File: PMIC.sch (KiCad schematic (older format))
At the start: 20 parts, among them J6 USB_B_Micro, U4 STPMIC1APQR

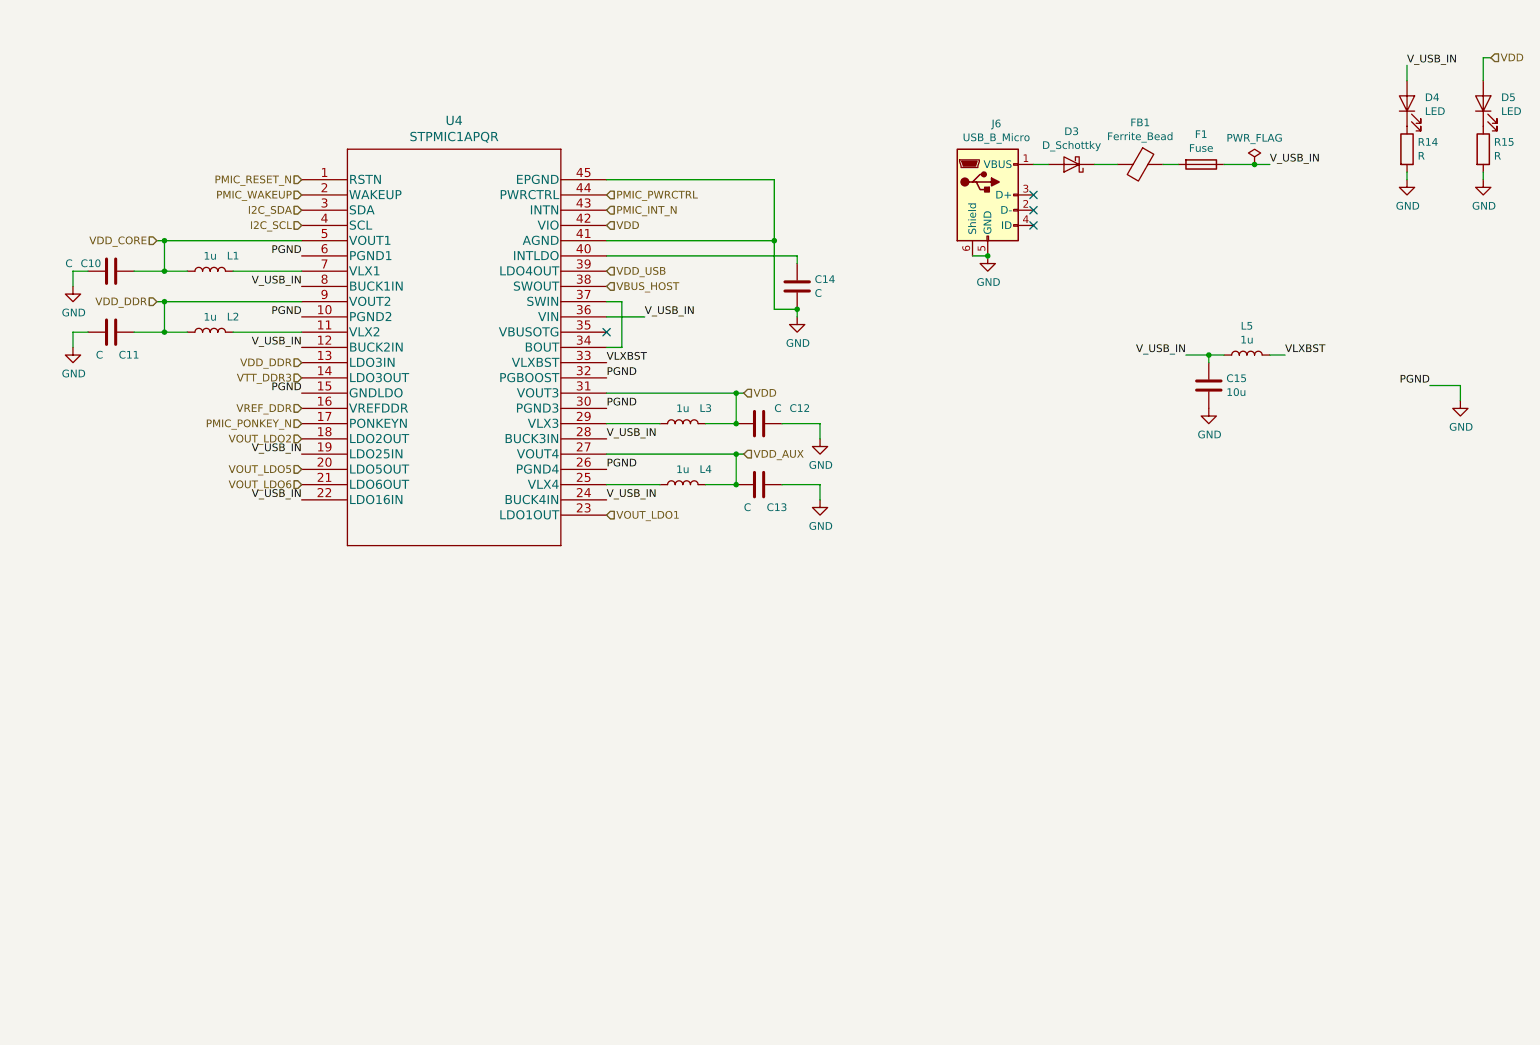
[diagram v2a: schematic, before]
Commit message: Complete ethernet and PMIC circuitry
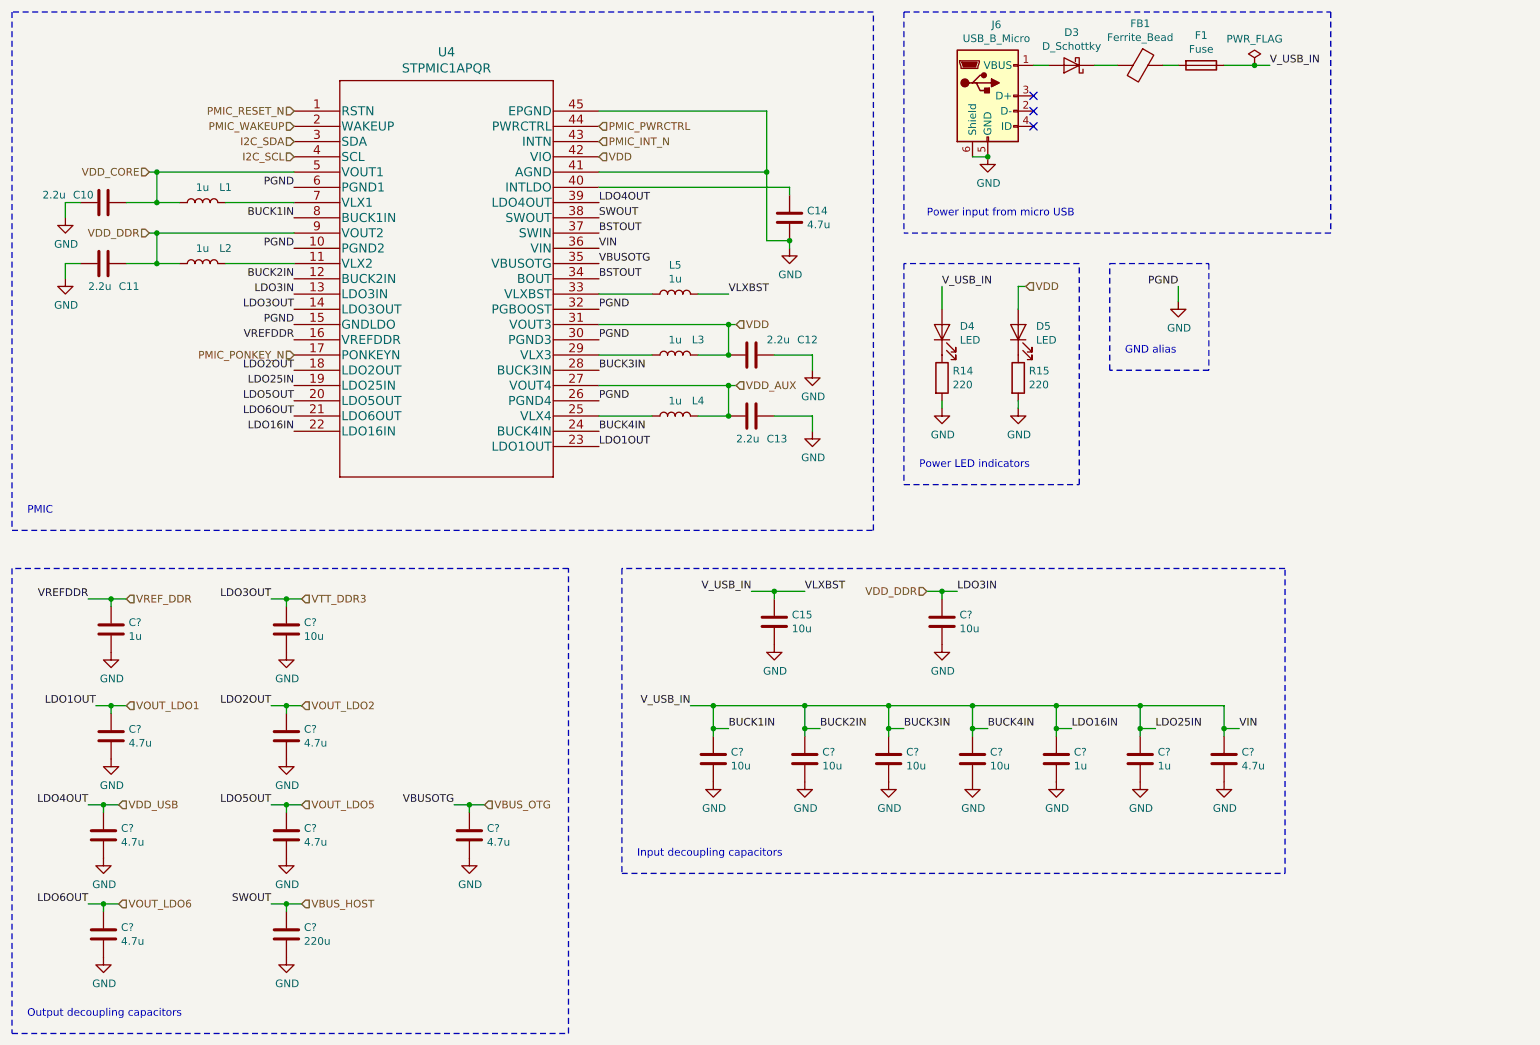
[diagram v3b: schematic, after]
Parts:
- added C? (x4): 10u, Capacitor_SMD:C_0603_1608Metric, symbol Device:C
- added C? (x7): 4.7u, symbol Device:C
- added C?: 220u, symbol Device:C
- added C? (x3): 1u, symbol Device:C
- added C? (x2): 10u, symbol Device:C
- C10, C11, C12, C13: value C -> 2.2u
- C14: value C -> 4.7u
- R14, R15: value R -> 220
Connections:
- net GND: now also C?.2, C?.2, C?.2, C?.2, C?.2, C?.2, C?.2, C?.2, C?.2, C?.2, C?.2, C?.2, C?.2, C?.2, C?.2, C?.2, C?.2
- net VBUS_HOST: now also C?.1
- net VDD_DDR: now also C?.1
- net VDD_USB: now also C?.1
- net VOUT_LDO1: now also C?.1
- net VOUT_LDO2: now also C?.1
- net VOUT_LDO5: now also C?.1
- net VOUT_LDO6: now also C?.1
- net VREF_DDR: now also C?.1
- net VTT_DDR3: now also C?.1
- net BSTOUT: now reaches U4.34 (BOUT), U4.37 (SWIN)
- net VBUS_OTG: now reaches U4.35 (VBUSOTG)
- net VBUS_OTG: now also C?.1
- net VLXBST: no longer names the net of U4.33 (VLXBST)
- net VLXBST: now also L5.1; no longer L5.2
- net V_USB_IN renamed BUCK1IN
- net BUCK1IN: now also L5.2, C?.1, C?.1, C?.1, C?.1, C?.1, C?.1, C?.1; no longer L5.1
- no-connect marks 4 -> 3
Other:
- note added: "GND alias\n"
- note added: "Input decoupling capacitors\n"
- note added: "Output decoupling capacitors"
- note added: "PMIC\n"
- note added: "Power LED indicators"
- note added: "Power input from micro USB"
- moved on the sheet: C10, C11, C12, C13, C14, C15, D3, D4, D5, F1, FB1, J6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

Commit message: Finish labelling RAM
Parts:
- gave numbers to parts that had none: 17
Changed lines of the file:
@@
 SWOUT
 $Comp
-L Device:C C?
+L Device:C C77
 U 1 1 616DE826
 P 5700 5650
-F 0 "C?" H 5815 5696 50  0000 L CNN
+F 0 "C77" H 5815 5696 50  0000 L CNN
 F 1 "10u" H 5815 5605 50  0000 L CNN
 F 2 "Capacitor_SMD:C_0603_1608Metric" H 5738 5500 50  0001 C CNN
@@
 V_USB_IN
 $Comp
-L power:GND #PWR?
+L power:GND #PWR0111
 U 1 1 616DE831
 P 5700 5800
-F 0 "#PWR?" H 5700 5550 50  0001 C CNN
+F 0 "#PWR0111" H 5700 5550 50  0001 C CNN
 F 1 "GND" H 5705 5627 50  0000 C CNN
 F 2 "" H 5700 5800 50  0001 C CNN
@@
 BUCK1IN
 $Comp
-L Device:C C?
+L Device:C C78
 U 1 1 616E9957
 P 6300 5650
-F 0 "C?" H 6415 5696 50  0000 L CNN
+F 0 "C78" H 6415 5696 50  0000 L CNN
 F 1 "10u" H 6415 5605 50  0000 L CNN
 F 2 "Capacitor_SMD:C_0603_1608Metric" H 6338 5500 50  0001 C CNN
@@
 	6300 5450 6400 5450
 $Comp
-L power:GND #PWR?
+L power:GND #PWR0112
 U 1 1 616E9962
 P 6300 5800
-F 0 "#PWR?" H 6300 5550 50  0001 C CNN
+F 0 "#PWR0112" H 6300 5550 50  0001 C CNN
 F 1 "GND" H 6305 5627 50  0000 C CNN
 F 2 "" H 6300 5800 50  0001 C CNN
@@
 Connection ~ 6300 5450
 $Comp
-L Device:C C?
+L Device:C C79
 U 1 1 616F4A5E
 P 6850 5650
-F 0 "C?" H 6965 5696 50  0000 L CNN
+F 0 "C79" H 6965 5696 50  0000 L CNN
 F 1 "10u" H 6965 5605 50  0000 L CNN
 F 2 "Capacitor_SMD:C_0603_1608Metric" H 6888 5500 50  0001 C CNN
@@
 	6850 5450 6950 5450
 $Comp
-L power:GND #PWR?
+L power:GND #PWR0113
 U 1 1 616F4A66
 P 6850 5800
-F 0 "#PWR?" H 6850 5550 50  0001 C CNN
+F 0 "#PWR0113" H 6850 5550 50  0001 C CNN
 F 1 "GND" H 6855 5627 50  0000 C CNN
 F 2 "" H 6850 5800 50  0001 C CNN
@@
 Connection ~ 6850 5450
 $Comp
-L Device:C C?
+L Device:C C81
 U 1 1 616F6459
 P 7400 5650
-F 0 "C?" H 7515 5696 50  0000 L CNN
+F 0 "C81" H 7515 5696 50  0000 L CNN
 F 1 "10u" H 7515 5605 50  0000 L CNN
 F 2 "Capacitor_SMD:C_0603_1608Metric" H 7438 5500 50  0001 C CNN
@@
 	7400 5450 7500 5450
 $Comp
-L power:GND #PWR?
+L power:GND #PWR0114
 U 1 1 616F6461
 P 7400 5800
-F 0 "#PWR?" H 7400 5550 50  0001 C CNN
+F 0 "#PWR0114" H 7400 5550 50  0001 C CNN
 F 1 "GND" H 7405 5627 50  0000 C CNN
 F 2 "" H 7400 5800 50  0001 C CNN
@@
 LDO1OUT
 $Comp
-L Device:C C?
+L Device:C C71
 U 1 1 61730A40
 P 1750 5500
-F 0 "C?" H 1865 5546 50  0000 L CNN
+F 0 "C71" H 1865 5546 50  0000 L CNN
 F 1 "4.7u" H 1865 5455 50  0000 L CNN
 F 2 "" H 1788 5350 50  0001 C CNN
@@
 Connection ~ 1750 5300
 $Comp
-L power:GND #PWR?
+L power:GND #PWR0115
 U 1 1 61734DB6
 P 1750 5650
-F 0 "#PWR?" H 1750 5400 50  0001 C CNN
+F 0 "#PWR0115" H 1750 5400 50  0001 C CNN
 F 1 "GND" H 1755 5477 50  0000 C CNN
 F 2 "" H 1750 5650 50  0001 C CNN
@@
 LDO2OUT
 $Comp
-L Device:C C?
+L Device:C C73
 U 1 1 6173BB67
 P 2900 5500
-F 0 "C?" H 3015 5546 50  0000 L CNN
+F 0 "C73" H 3015 5546 50  0000 L CNN
 F 1 "4.7u" H 3015 5455 50  0000 L CNN
 F 2 "" H 2938 5350 50  0001 C CNN
@@
 Connection ~ 2900 5300
 $Comp
-L power:GND #PWR?
+L power:GND #PWR0116
 U 1 1 6173BB71
 P 2900 5650
-F 0 "#PWR?" H 2900 5400 50  0001 C CNN
+F 0 "#PWR0116" H 2900 5400 50  0001 C CNN
 F 1 "GND" H 2905 5477 50  0000 C CNN
 F 2 "" H 2900 5650 50  0001 C CNN
@@
 LDO4OUT
 $Comp
-L Device:C C?
+L Device:C C68
 U 1 1 6174297D
 P 1700 6150
-F 0 "C?" H 1815 6196 50  0000 L CNN
+F 0 "C68" H 1815 6196 50  0000 L CNN
 F 1 "4.7u" H 1815 6105 50  0000 L CNN
 F 2 "" H 1738 6000 50  0001 C CNN
@@
 Connection ~ 1700 5950
 $Comp
-L power:GND #PWR?
+L power:GND #PWR0117
 U 1 1 61742987
 P 1700 6300
-F 0 "#PWR?" H 1700 6050 50  0001 C CNN
+F 0 "#PWR0117" H 1700 6050 50  0001 C CNN
 F 1 "GND" H 1705 6127 50  0000 C CNN
 F 2 "" H 1700 6300 50  0001 C CNN
@@
 LDO5OUT
 $Comp
-L Device:C C?
+L Device:C C74
 U 1 1 6174E104
 P 2900 6150
-F 0 "C?" H 3015 6196 50  0000 L CNN
+F 0 "C74" H 3015 6196 50  0000 L CNN
 F 1 "4.7u" H 3015 6105 50  0000 L CNN
 F 2 "" H 2938 6000 50  0001 C CNN
@@
 Connection ~ 2900 5950
 $Comp
-L power:GND #PWR?
+L power:GND #PWR0118
 U 1 1 6174E10E
 P 2900 6300
-F 0 "#PWR?" H 2900 6050 50  0001 C CNN
+F 0 "#PWR0118" H 2900 6050 50  0001 C CNN
 F 1 "GND" H 2905 6127 50  0000 C CNN
 F 2 "" H 2900 6300 50  0001 C CNN
@@
 LDO6OUT
 $Comp
-L Device:C C?
+L Device:C C69
 U 1 1 61764604
 P 1700 6800
-F 0 "C?" H 1815 6846 50  0000 L CNN
+F 0 "C69" H 1815 6846 50  0000 L CNN
 F 1 "4.7u" H 1815 6755 50  0000 L CNN
 F 2 "" H 1738 6650 50  0001 C CNN
@@
 Connection ~ 1700 6600
 $Comp
-L power:GND #PWR?
+L power:GND #PWR0119
 U 1 1 6176460E
 P 1700 6950
-F 0 "#PWR?" H 1700 6700 50  0001 C CNN
+F 0 "#PWR0119" H 1700 6700 50  0001 C CNN
 F 1 "GND" H 1705 6777 50  0000 C CNN
 F 2 "" H 1700 6950 50  0001 C CNN
@@
 SWOUT
 $Comp
-L Device:C C?
+L Device:C C75
 U 1 1 6178B094
 P 2900 6800
-F 0 "C?" H 3015 6846 50  0000 L CNN
+F 0 "C75" H 3015 6846 50  0000 L CNN
 F 1 "220u" H 3015 6755 50  0000 L CNN
 F 2 "" H 2938 6650 50  0001 C CNN
@@
 Connection ~ 2900 6600
 $Comp
-L power:GND #PWR?
+L power:GND #PWR0120
 U 1 1 6178B09E
 P 2900 6950
-F 0 "#PWR?" H 2900 6700 50  0001 C CNN
+F 0 "#PWR0120" H 2900 6700 50  0001 C CNN
 F 1 "GND" H 2905 6777 50  0000 C CNN
 F 2 "" H 2900 6950 50  0001 C CNN
@@
 VREFDDR
 $Comp
-L Device:C C?
+L Device:C C70
 U 1 1 617ABEFC
 P 1750 4800
-F 0 "C?" H 1865 4846 50  0000 L CNN
+F 0 "C70" H 1865 4846 50  0000 L CNN
 F 1 "1u" H 1865 4755 50  0000 L CNN
 F 2 "" H 1788 4650 50  0001 C CNN
@@
 $EndComp
 $Comp
-L power:GND #PWR?
+L power:GND #PWR0121
 U 1 1 617AC761
 P 1750 4950
-F 0 "#PWR?" H 1750 4700 50  0001 C CNN
+F 0 "#PWR0121" H 1750 4700 50  0001 C CNN
 F 1 "GND" H 1755 4777 50  0000 C CNN
 F 2 "" H 1750 4950 50  0001 C CNN
@@
 LDO16IN
 $Comp
-L Device:C C?
+L Device:C C82
 U 1 1 617D2D60
 P 7950 5650
-F 0 "C?" H 8065 5696 50  0000 L CNN
+F 0 "C82" H 8065 5696 50  0000 L CNN
 F 1 "1u" H 8065 5605 50  0000 L CNN
 F 2 "" H 7988 5500 50  0001 C CNN
@@
 Connection ~ 7400 5300
 $Comp
-L power:GND #PWR?
+L power:GND #PWR0122
 U 1 1 617D97E2
 P 7950 5800
-F 0 "#PWR?" H 7950 5550 50  0001 C CNN
+F 0 "#PWR0122" H 7950 5550 50  0001 C CNN
 F 1 "GND" H 7955 5627 50  0000 C CNN
 F 2 "" H 7950 5800 50  0001 C CNN
@@
 LDO25IN
 $Comp
-L Device:C C?
+L Device:C C83
 U 1 1 617DAEA7
 P 8500 5650
-F 0 "C?" H 8615 5696 50  0000 L CNN
+F 0 "C83" H 8615 5696 50  0000 L CNN
 F 1 "1u" H 8615 5605 50  0000 L CNN
 F 2 "" H 8538 5500 50  0001 C CNN
@@
 Connection ~ 8500 5450
 $Comp
-L power:GND #PWR?
+L power:GND #PWR0123
 U 1 1 617DAEB2
 P 8500 5800
-F 0 "#PWR?" H 8500 5550 50  0001 C CNN
+F 0 "#PWR0123" H 8500 5550 50  0001 C CNN
 F 1 "GND" H 8505 5627 50  0000 C CNN
 F 2 "" H 8500 5800 50  0001 C CNN
@@
 LDO3OUT
 $Comp
-L Device:C C?
+L Device:C C72
 U 1 1 617F9E6E
 P 2900 4800
-F 0 "C?" H 3015 4846 50  0000 L CNN
+F 0 "C72" H 3015 4846 50  0000 L CNN
 F 1 "10u" H 3015 4755 50  0000 L CNN
 F 2 "" H 2938 4650 50  0001 C CNN
@@
 Connection ~ 2900 4600
 $Comp
-L power:GND #PWR?
+L power:GND #PWR0124
 U 1 1 617F9E78
 P 2900 4950
-F 0 "#PWR?" H 2900 4700 50  0001 C CNN
+F 0 "#PWR0124" H 2900 4700 50  0001 C CNN
 F 1 "GND" H 2905 4777 50  0000 C CNN
 F 2 "" H 2900 4950 50  0001 C CNN
@@
 VDD_DDR
 $Comp
-L Device:C C?
+L Device:C C80
 U 1 1 61818B9A
 P 7200 4750
-F 0 "C?" H 7315 4796 50  0000 L CNN
+F 0 "C80" H 7315 4796 50  0000 L CNN
 F 1 "10u" H 7315 4705 50  0000 L CNN
 F 2 "" H 7238 4600 50  0001 C CNN
@@
 Connection ~ 7200 4550
 $Comp
-L power:GND #PWR?
+L power:GND #PWR0125
 U 1 1 61818BA4
 P 7200 4900
-F 0 "#PWR?" H 7200 4650 50  0001 C CNN
+F 0 "#PWR0125" H 7200 4650 50  0001 C CNN
 F 1 "GND" H 7205 4727 50  0000 C CNN
 F 2 "" H 7200 4900 50  0001 C CNN
@@
 VIN
 $Comp
-L Device:C C?
+L Device:C C84
 U 1 1 6184CE28
 P 9050 5650
-F 0 "C?" H 9165 5696 50  0000 L CNN
+F 0 "C84" H 9165 5696 50  0000 L CNN
 F 1 "4.7u" H 9165 5605 50  0000 L CNN
 F 2 "" H 9088 5500 50  0001 C CNN
@@
 Connection ~ 9050 5450
 $Comp
-L power:GND #PWR?
+L power:GND #PWR0126
 U 1 1 6184CE33
 P 9050 5800
-F 0 "#PWR?" H 9050 5550 50  0001 C CNN
+F 0 "#PWR0126" H 9050 5550 50  0001 C CNN
 F 1 "GND" H 9055 5627 50  0000 C CNN
 F 2 "" H 9050 5800 50  0001 C CNN
@@
 VBUS_OTG
 $Comp
-L Device:C C?
+L Device:C C76
 U 1 1 618A2F29
 P 4100 6150
-F 0 "C?" H 4215 6196 50  0000 L CNN
+F 0 "C76" H 4215 6196 50  0000 L CNN
 F 1 "4.7u" H 4215 6105 50  0000 L CNN
 F 2 "" H 4138 6000 50  0001 C CNN
@@
 Connection ~ 4100 5950
 $Comp
-L power:GND #PWR?
+L power:GND #PWR0127
 U 1 1 618A2F33
 P 4100 6300
-F 0 "#PWR?" H 4100 6050 50  0001 C CNN
+F 0 "#PWR0127" H 4100 6050 50  0001 C CNN
 F 1 "GND" H 4105 6127 50  0000 C CNN
 F 2 "" H 4100 6300 50  0001 C CNN

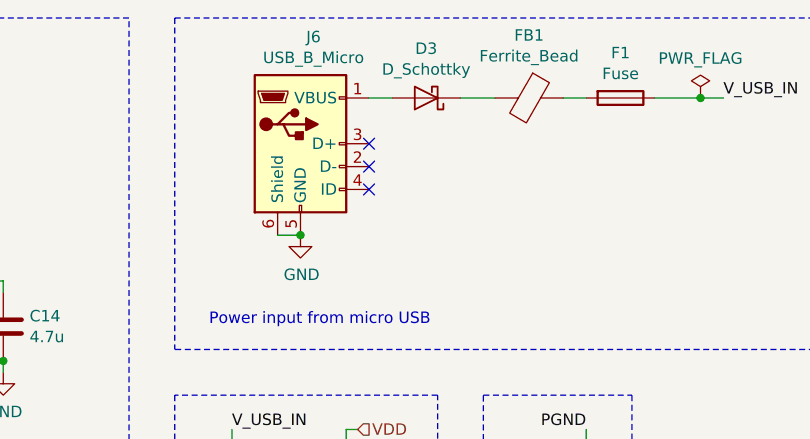
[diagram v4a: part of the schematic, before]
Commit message: Complete gpio selection, tidy sheets
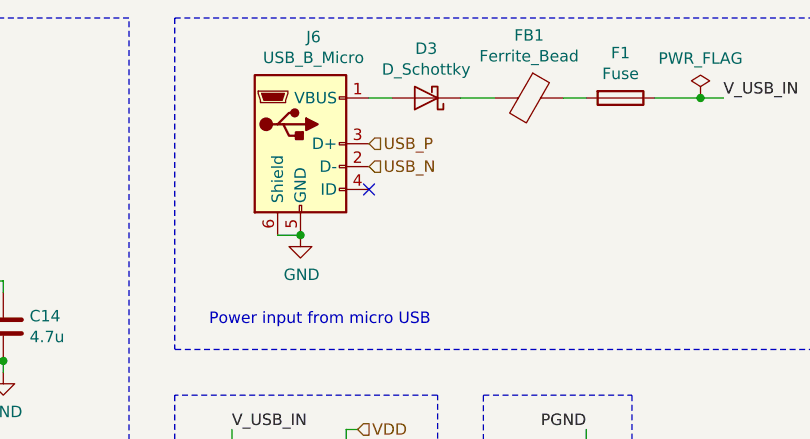
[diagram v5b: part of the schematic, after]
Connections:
- net USB_N: now reaches J6.2 (D-)
- net USB_P: now reaches J6.3 (D+)
- no-connect marks 3 -> 1
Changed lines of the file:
@@
 	7400 1700 7500 1700
 NoConn ~ 7800 1500
-NoConn ~ 7800 1400
-NoConn ~ 7800 1300
 $Comp
 L power:GND #PWR?
@@
 Wire Notes Line
 	1100 750  1100 4150
+Text HLabel 7800 1300 2    50   Input ~ 0
+USB_P
+Text HLabel 7800 1400 2    50   Input ~ 0
+USB_N
 $EndSCHEMATC
